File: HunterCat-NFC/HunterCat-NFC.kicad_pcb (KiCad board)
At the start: 2 copper layers, 108 x 53.8 mm, 65 parts, among them J1 Battery, J2 Breakout Conn, P1 USB_C_Plug_USB2.0, SW1 RESET, U1 ATSAMD21E18A, U2 PN7150B0HN_C11002E-PN7150B0HN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, U3 MCP73831-3-OT, U4 AP2112K-3.3, U5 W25Q32JVSS, Y1 27.12Mhz

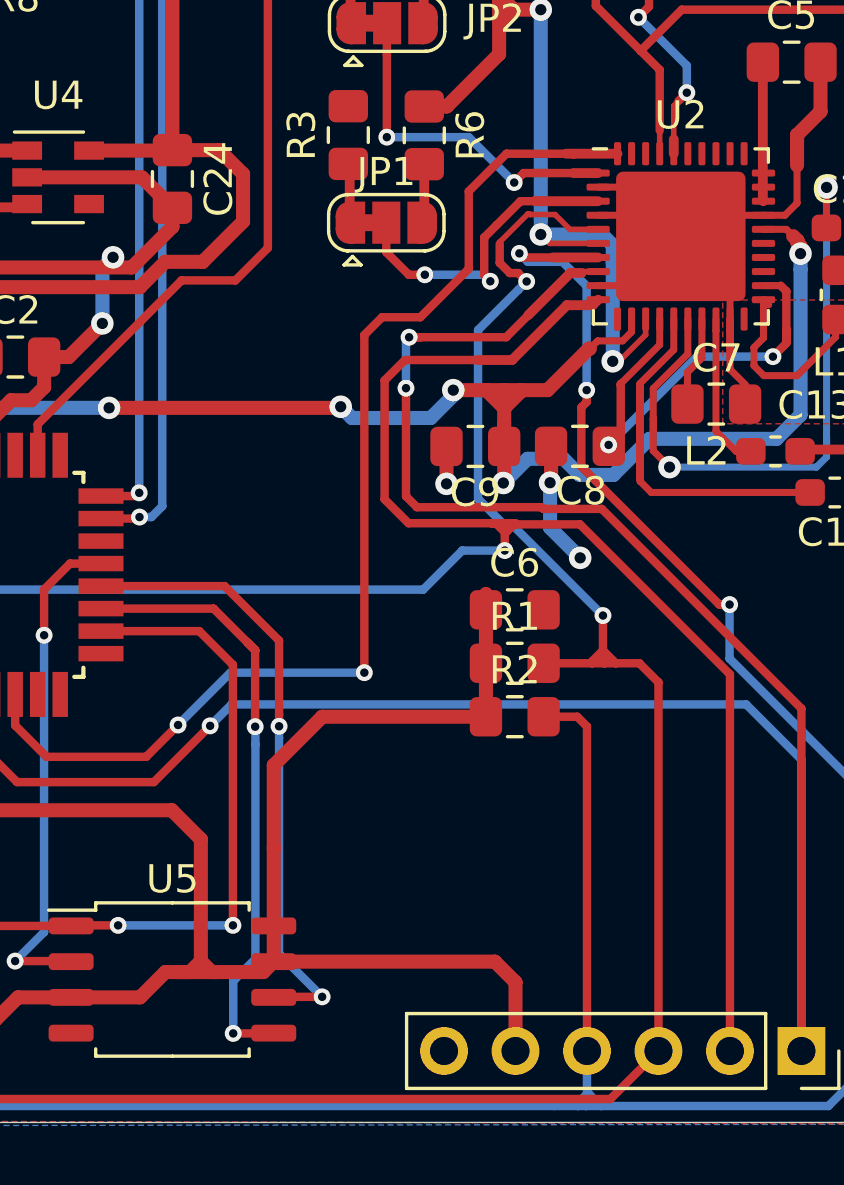
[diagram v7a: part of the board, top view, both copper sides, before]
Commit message: add c25
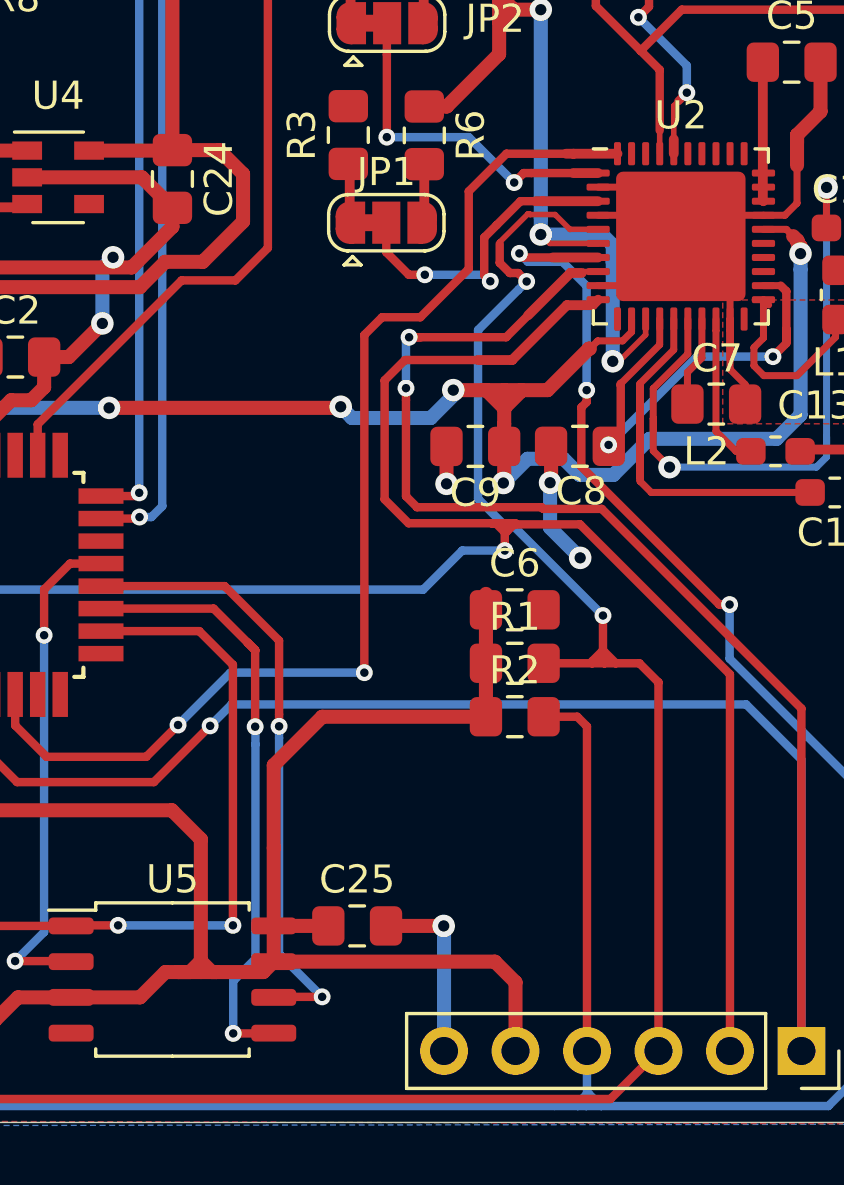
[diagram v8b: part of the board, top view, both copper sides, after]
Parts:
- added C25: 10uF, Capacitor_SMD:C_0805_2012Metric_Pad1.15x1.40mm_HandSolder, F.Cu at (137.4, 120.3)
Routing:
- net GND: track 97.0 -> 103.5 mm, vias 9 -> 10
- net +3V3: track 161.8 -> 163.7 mm
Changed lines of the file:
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@@
     (thickness 1.6)
     (drawings 7)
-    (tracks 723)
+    (tracks 729)
     (zones 0)
-    (modules 65)
+    (modules 66)
     (nets 68)
   )
@@
     (company "Electronic Cats")
     (comment 1 "Eduardo Contreras")
+    (comment 2 "Montserrat Figueroa ")
   )
   (layers
@@
     (add_net VBUS)
   )
+  (module Capacitor_SMD:C_0805_2012Metric_Pad1.15x1.40mm_HandSolder (layer F.Cu)
+    (at 137.375 120.27)
+    (descr "Capacitor SMD 0805 (2012 Metric), square (rectangular) end terminal, IPC_7351 nominal with elongated pad for handsoldering. (Body size source: https://docs.google.com/spreadsheets/d/1BsfQQcO9C6DZCsRaXUlFlo91Tg2WpOkGARC1WS5S8t0/edit?usp=sharing), generated with kicad-footprint-generator")
+    (tags "capacitor handsolder")
+    (attr smd)
+    (fp_text reference C25 (at 0 -1.65) (layer F.SilkS)
+      (effects (font (size 1 1) (thickness 0.15)))
+    )
+    (fp_text value 10uF (at 0 1.65) (layer F.Fab)
+      (effects (font (size 1 1) (thickness 0.15)))
+    )
+    (fp_text user %R (at 0 0) (layer F.Fab)
+      (effects (font (size 0.5 0.5) (thickness 0.08)))
+    )
+    (fp_line (start 1.85 0.95) (end -1.85 0.95) (layer F.CrtYd) (width 0.05))
+    (fp_line (start 1.85 -0.95) (end 1.85 0.95) (layer F.CrtYd) (width 0.05))
+    (fp_line (start -1.85 -0.95) (end 1.85 -0.95) (layer F.CrtYd) (width 0.05))
+    (fp_line (start -1.85 0.95) (end -1.85 -0.95) (layer F.CrtYd) (width 0.05))
+    (fp_line (start -0.261252 0.71) (end 0.261252 0.71) (layer F.SilkS) (width 0.12))
+    (fp_line (start -0.261252 -0.71) (end 0.261252 -0.71) (layer F.SilkS) (width 0.12))
+    (fp_line (start 1 0.6) (end -1 0.6) (layer F.Fab) (width 0.1))
+    (fp_line (start 1 -0.6) (end 1 0.6) (layer F.Fab) (width 0.1))
+    (fp_line (start -1 -0.6) (end 1 -0.6) (layer F.Fab) (width 0.1))
+    (fp_line (start -1 0.6) (end -1 -0.6) (layer F.Fab) (width 0.1))
+    (pad 2 smd roundrect (at 1.025 0) (size 1.15 1.4) (layers F.Cu F.Paste F.Mask) (roundrect_rratio 0.217391)
+      (net 1 GND))
+    (pad 1 smd roundrect (at -1.025 0) (size 1.15 1.4) (layers F.Cu F.Paste F.Mask) (roundrect_rratio 0.217391)
+      (net 2 +3V3))
+    (model ${KISYS3DMOD}/Capacitor_SMD.3dshapes/C_0805_2012Metric.wrl
+      (at (xyz 0 0 0))
+      (scale (xyz 1 1 1))
+      (rotate (xyz 0 0 0))
+    )
+  )
   (module Crystal:Crystal_SMD_3225-4Pin_3.2x2.5mm_HandSoldering (layer F.Cu)
     (at 153.692 84.828)
@@
   (segment (start 128.32 96.89) (end 128.7 96.51) (width 0.5) (layer B.Cu) (net 1))
   (segment (start 128.32 98.86) (end 128.32 96.89) (width 0.5) (layer B.Cu) (net 1))
+  (via (at 140.45 120.27) (size 0.8) (drill 0.4) (layers F.Cu B.Cu) (net 1))
+  (segment (start 140.462 120.282) (end 140.45 120.27) (width 0.5) (layer B.Cu) (net 1))
+  (segment (start 140.462 124.714) (end 140.462 120.282) (width 0.5) (layer B.Cu) (net 1))
+  (segment (start 140.45 120.27) (end 138.4 120.27) (width 0.5) (layer F.Cu) (net 1))
   (segment (start 143.002 122.272) (end 142.269 121.539) (width 0.5) (layer F.Cu) (net 2))
   (segment (start 143.002 124.714) (end 143.002 122.272) (width 0.5) (layer F.Cu) (net 2))
@@
   (segment (start 122.822 98.708) (end 122.822 103.544) (width 0.5) (layer F.Cu) (net 2))
   (segment (start 123.899989 97.630011) (end 122.822 98.708) (width 0.5) (layer F.Cu) (net 2))
+  (segment (start 136.349 120.269) (end 136.35 120.27) (width 0.5) (layer F.Cu) (net 2))
+  (segment (start 134.41 120.269) (end 136.349 120.269) (width 0.5) (layer F.Cu) (net 2))
   (segment (start 123.578628 103.500628) (end 123.622 103.544) (width 0.3) (layer F.Cu) (net 3))
   (segment (start 124.202 101.308) (end 123.578628 101.931372) (width 0.3) (layer F.Cu) (net 3))
@@
   (segment (start 137.11 93.24) (end 137.06 93.19) (width 0.35) (layer F.Cu) (net 25))
   (segment (start 137.11 95.28) (end 137.11 93.24) (width 0.35) (layer F.Cu) (net 25))
-  (segment (start 143.716 94.516) (end 143.7 94.5) (width 0.35) (layer F.Cu) (net 26))
   (via (at 139.78 97.13) (size 0.6) (drill 0.3) (layers F.Cu B.Cu) (net 26))
   (segment (start 139.21 97.13) (end 139.78 97.13) (width 0.3) (layer F.Cu) (net 26))
@@
   (segment (start 137.14 86.16) (end 137.09 86.11) (width 0.35) (layer F.Cu) (net 28))
   (segment (start 137.14 88.19) (end 137.14 86.16) (width 0.35) (layer F.Cu) (net 28))
-  (segment (start 145.9385 93.516) (end 145.05499 93.516) (width 0.35) (layer F.Cu) (net 29))
   (segment (start 138.43 88.2) (end 138.44 88.19) (width 0.3) (layer F.Cu) (net 29))
   (via (at 138.43 92.24) (size 0.6) (drill 0.3) (layers F.Cu B.Cu) (net 29))
@@
   (via (at 142.954347 93.853412) (size 0.6) (drill 0.3) (layers F.Cu B.Cu) (net 29))
   (segment (start 141.340935 92.24) (end 142.954347 93.853412) (width 0.3) (layer B.Cu) (net 29))
-  (segment (start 143.291759 93.516) (end 142.954347 93.853412) (width 0.3) (layer F.Cu) (net 29))
-  (segment (start 145.05499 93.516) (end 143.291759 93.516) (width 0.3) (layer F.Cu) (net 29))
+  (segment (start 143.291759 93.516) (end 143.564 93.516) (width 0.3) (layer F.Cu) (net 29))
+  (segment (start 142.954347 93.853412) (end 143.291759 93.516) (width 0.3) (layer F.Cu) (net 29))
+  (segment (start 145.05499 93.516) (end 143.564 93.516) (width 0.3) (layer F.Cu) (net 29))
+  (segment (start 145.9385 93.516) (end 145.05499 93.516) (width 0.35) (layer F.Cu) (net 29))
   (segment (start 139.74 86.195) (end 139.8 86.135) (width 0.35) (layer F.Cu) (net 30))
   (segment (start 139.74 88.19) (end 139.74 86.195) (width 0.35) (layer F.Cu) (net 30))
